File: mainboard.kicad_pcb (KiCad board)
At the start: 4 copper layers, 94.4 x 36.2 mm, 48 parts, among them IC1 BMX160, J1 Conn_01x01, J2 10118194-0001LF, J28 Conn_01x01, J29 Conn_01x01, J3 Micro_SD_Card, J30 Conn_01x01, J4 xf2m-2415-1a, J5 XF2M-1015-1A, SW1 KMR231NG LFS, U1 RFM95W-915S2, U2 ATSAMD51G_TQFN48, U3 DRV8848, U4 TPS82740BSIPR, U5 DRV8848, U6 MAX708RESA-T, U8 RFM95W-915S2, X1 ANTENNA_U.FL, X2 ANTENNA_U.FL

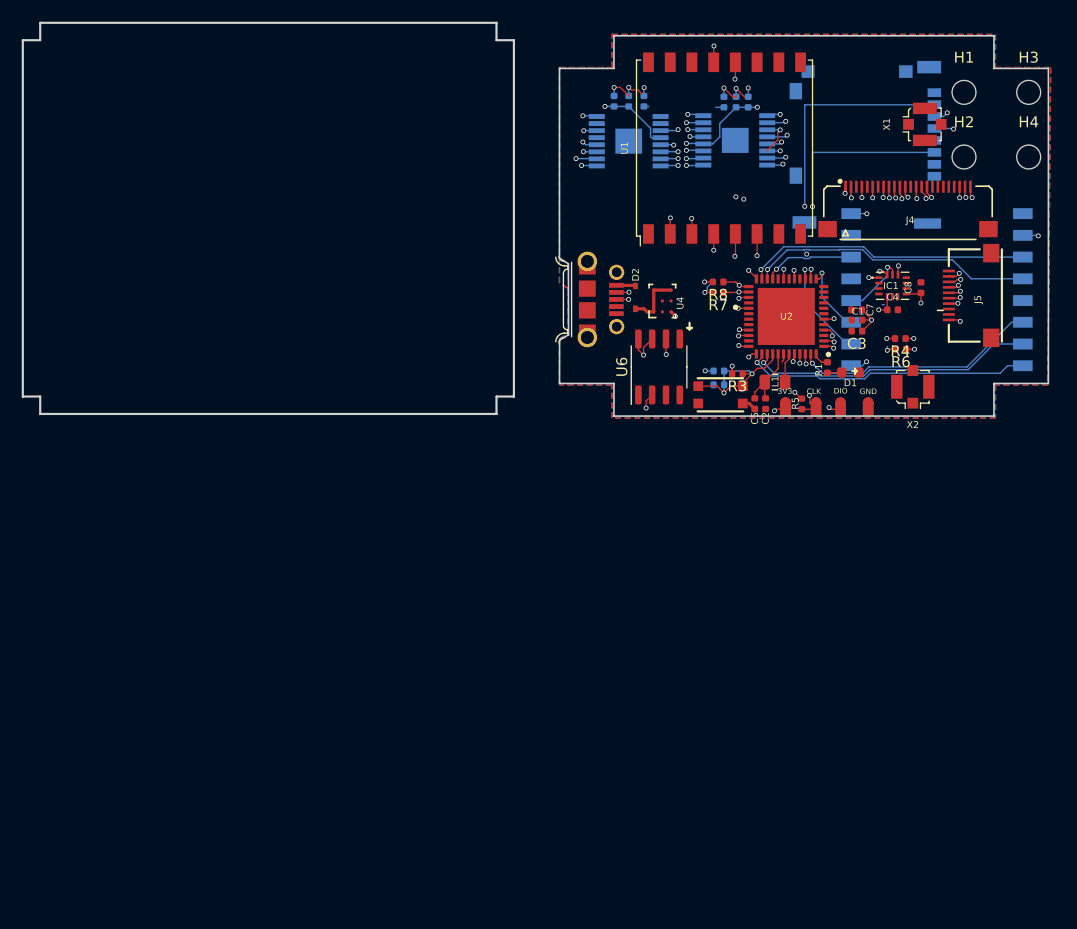
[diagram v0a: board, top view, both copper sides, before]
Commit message: modified board outline based on update from mechanical, including USB slot
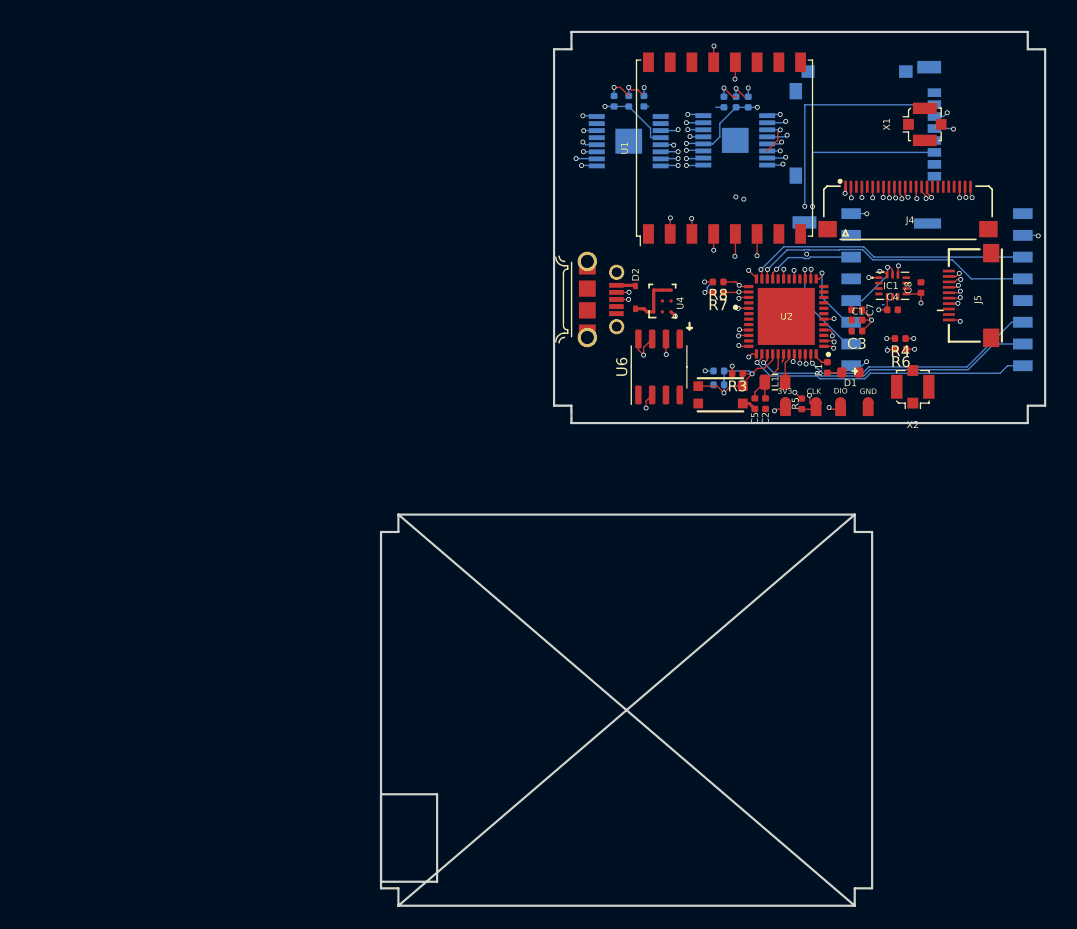
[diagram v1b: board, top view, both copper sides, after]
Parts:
- removed H1, H2, H3, H4: MountingHole, MountingHole:MountingHole_2.2mm_M2
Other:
- board size 94.4 x 36.2 mm -> 61.1 x 80.4 mm

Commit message: updated edge cuts to match updated mechanical .dxf file (to allow flat flex connectors to travel around board edge)
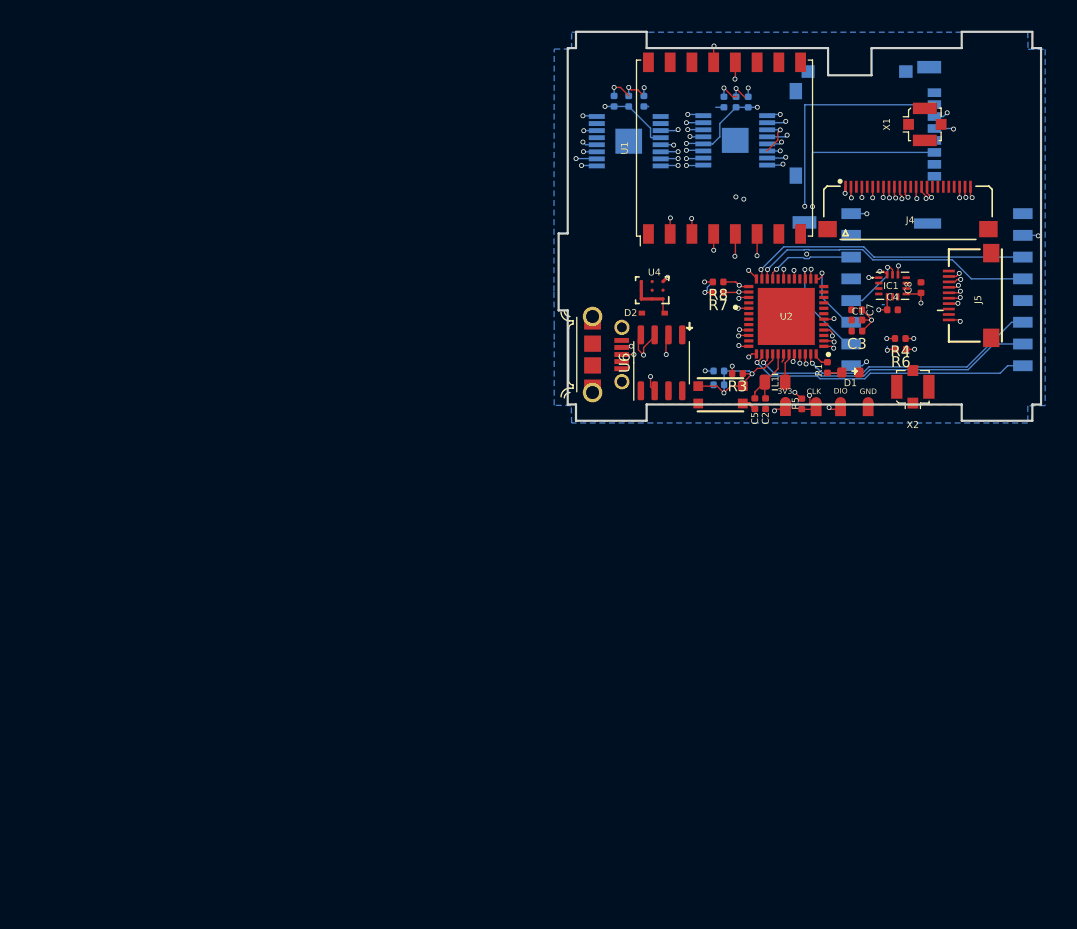
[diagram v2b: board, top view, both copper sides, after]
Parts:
- moved J2 5.09 mm to (79.8, 103.4)
- moved D2 2.19 mm to (85.3, 99.6), turned to 180 degrees
- moved U4 1.37 mm to (85.2, 97.5), turned to 180 degrees
- moved U6 0.44 mm to (86.1, 104.1)
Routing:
- net VUSB: track 1.78 -> 0.45 mm
- net /USB+: track 13.8 -> 12.7 mm
- net /USB-: track 14.1 -> 13.1 mm
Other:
- board size 61.1 x 80.4 mm -> 44.4 x 35.8 mm

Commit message: Updated component placement on top and bottom faces (no traces)
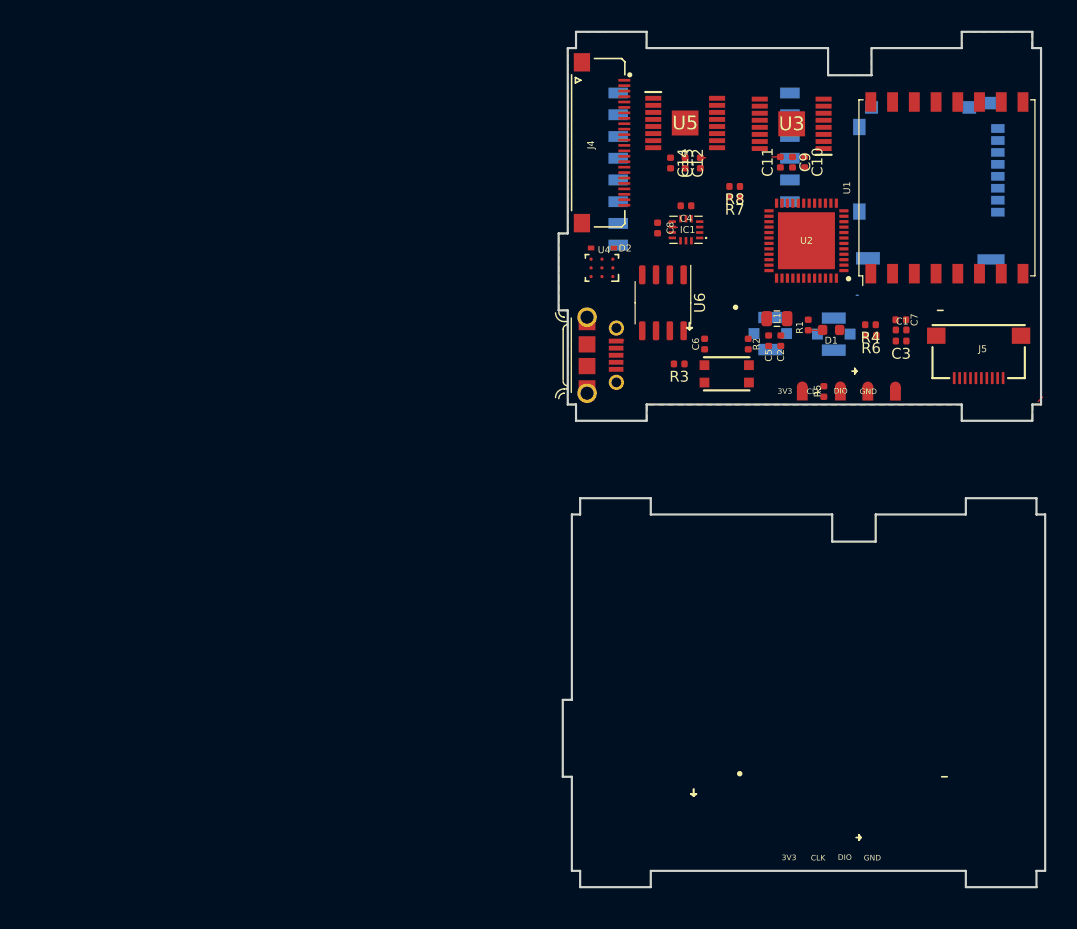
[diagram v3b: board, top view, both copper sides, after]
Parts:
- C10, C11, C12, C13, C14, C6, C9, R2, U3, U5: moved to F.Cu
- X1, X2: moved to B.Cu
- moved J4 26.4 mm to (82.7, 83.9), turned to 270 degrees
- moved C8 24.9 mm to (85.7, 91.7), turned to 270 degrees
- moved U8 24.1 mm to (90.0, 86.3)
- moved X1 23.9 mm to (96.1, 101.4), turned to 90 degrees
- moved C4 21.3 mm to (88.4, 89.7), turned to 180 degrees
- moved U1 20.8 mm to (112.4, 88.0)
- moved IC1 19.7 mm to (88.4, 91.9), turned to 0 degrees
- moved R7 8.92 mm to (92.8, 88.9)
- moved R8 8.92 mm to (92.8, 87.9)
- moved X2 8.75 mm to (102.0, 101.5), turned to 270 degrees
- moved J5 8.09 mm to (115.3, 105.5), turned to 180 degrees
- moved C12 7.70 mm to (88.3, 85.8), turned to 270 degrees
- moved C13 7.70 mm to (89.7, 85.8), turned to 90 degrees
- moved C14 7.70 mm to (86.9, 85.8), turned to 270 degrees
- moved D2 7.60 mm to (80.7, 93.6), turned to 0 degrees
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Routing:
- net BATT_P: track 72.4 -> 0.07 mm, vias 5 -> 0
- net MISO: track 68.2 -> 0.00 mm, vias 5 -> 0
- net MOSI: track 57.7 -> 0.00 mm, vias 5 -> 0
- net SCK: track 49.5 -> 0.00 mm, vias 6 -> 0
- net MOY_2: track 31.4 -> 0.00 mm, vias 2 -> 0
- net MOY_1: track 30.7 -> 0.04 mm, vias 2 -> 0
- net +3V3: track 30.9 -> 1.85 mm, vias 21 -> 0
- net GND: track 29.5 -> 0.64 mm, vias 17 -> 0
- net RF_DIO1: track 26.6 -> 0.00 mm, vias 1 -> 0
- net RF_DIO2: track 26.5 -> 0.00 mm, vias 1 -> 0
- net RF_BUSY: track 26.3 -> 0.00 mm, vias 1 -> 0
- net RF_DIO3: track 26.3 -> 0.00 mm, vias 1 -> 0
- net SDA1: track 25.2 -> 0.00 mm, vias 3 -> 0
- net SCL1: track 23.9 -> 0.00 mm, vias 3 -> 0
- net EN_CAM: track 22.9 -> 0.00 mm, vias 2 -> 0
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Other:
- board size 44.4 x 35.8 mm -> 44.8 x 78.7 mm

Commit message: updated layout with new camera connector placement, more traces, removed mounting holes
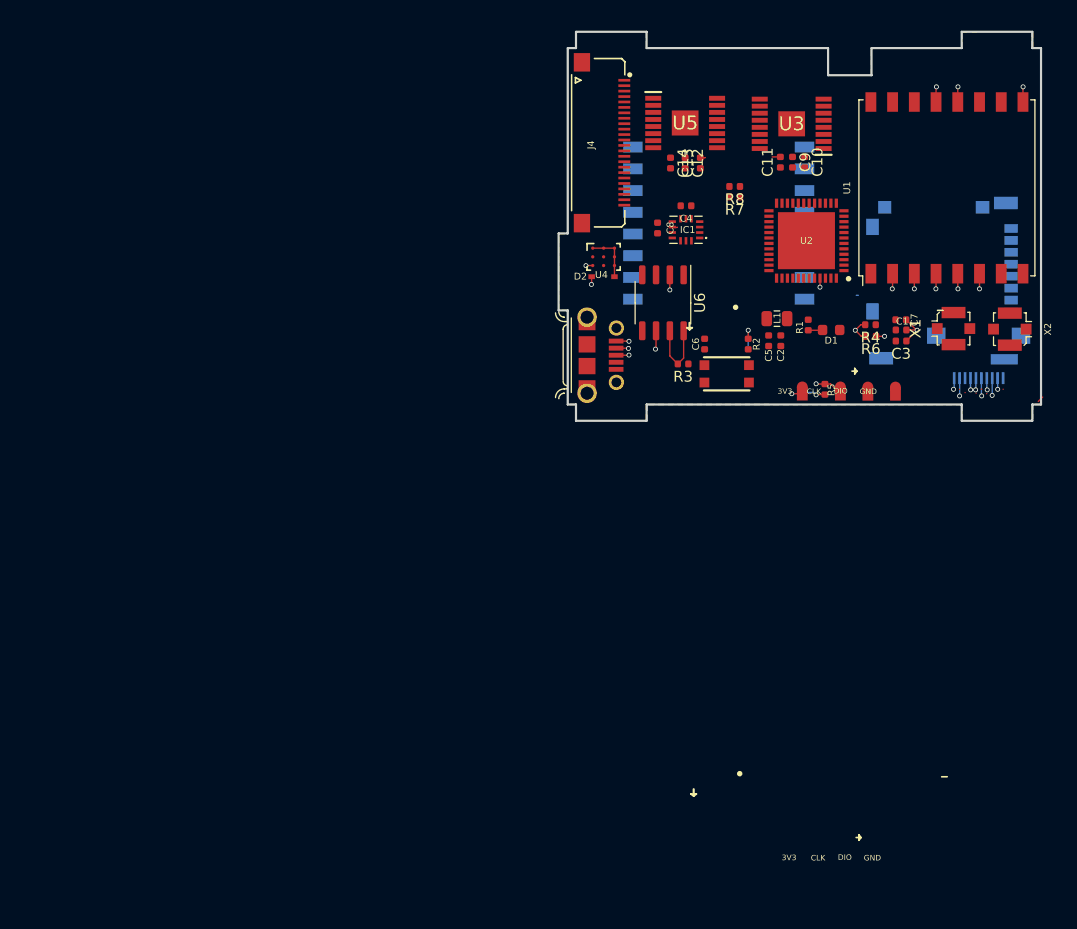
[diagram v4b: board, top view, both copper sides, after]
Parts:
- J5: moved to B.Cu
- X1, X2: moved to F.Cu
- moved X1 16.9 mm to (113.0, 101.0), turned to 270 degrees
- moved X2 16.2 mm to (118.2, 101.0), turned to 90 degrees
- moved J3 9.28 mm to (112.7, 96.6)
- moved U8 5.15 mm to (91.4, 91.3)
- moved D2 2.64 mm to (80.7, 96.2), turned to 180 degrees
- moved U4 1.03 mm to (80.8, 94.4), turned to 0 degrees
- moved R3 0.36 mm to (88.1, 104.2)
- moved R5 0.23 mm to (101.1, 106.6), turned to 90 degrees
- moved R6 0.08 mm to (105.4, 101.7)
- turned J5 to 0 degrees
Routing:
- net +3V3: track 1.85 -> 17.2 mm, vias 0 -> 8
- net Net-(R3-Pad2): track 0.00 -> 6.63 mm
- net Net-(D2-Pad1): track 0.00 -> 4.63 mm
- net /SWCLK: track 0.00 -> 3.44 mm, vias 0 -> 2
- net MOSI: track 0.00 -> 2.99 mm, vias 0 -> 2
- net MISO: track 0.00 -> 2.50 mm, vias 0 -> 2
- net SCK: track 0.00 -> 2.44 mm, vias 0 -> 2
- net WDT_WDI: track 0.00 -> 1.71 mm, vias 0 -> 1
- net CS_CAM: track 0.00 -> 1.65 mm, vias 0 -> 1
- net GND: track 0.64 -> 2.28 mm, vias 0 -> 1
- net VUSB: track 0.45 -> 1.91 mm, vias 0 -> 2
- net RF2_BUSY: track 0.00 -> 1.40 mm, vias 0 -> 1
- net CS_RF2: track 0.00 -> 1.40 mm, vias 0 -> 1
- net Net-(U1-Pad9): track 0.00 -> 1.40 mm, vias 0 -> 1
- net RF2_RST: track 0.00 -> 1.40 mm, vias 0 -> 1
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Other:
- board size 44.8 x 78.7 mm -> 44.4 x 35.8 mm

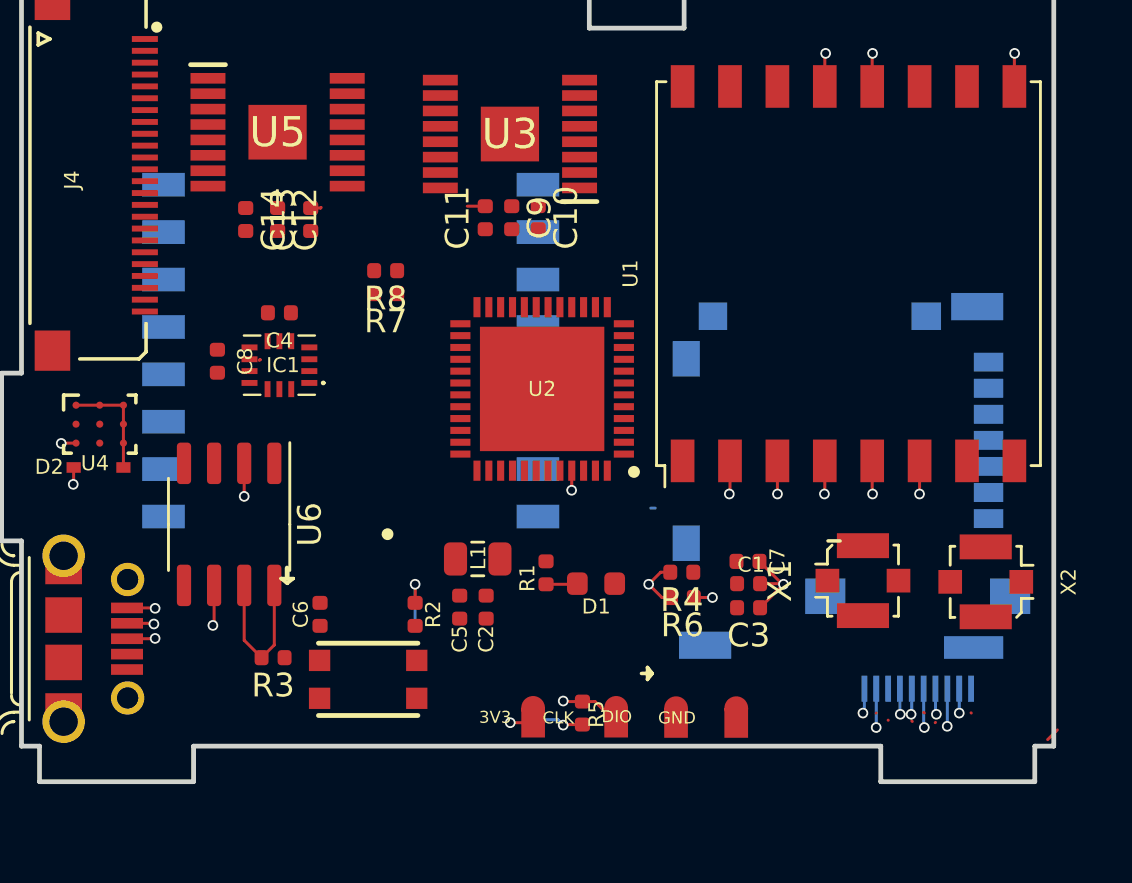
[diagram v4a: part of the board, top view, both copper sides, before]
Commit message: updated footprints for U.FL connectors, more traces added
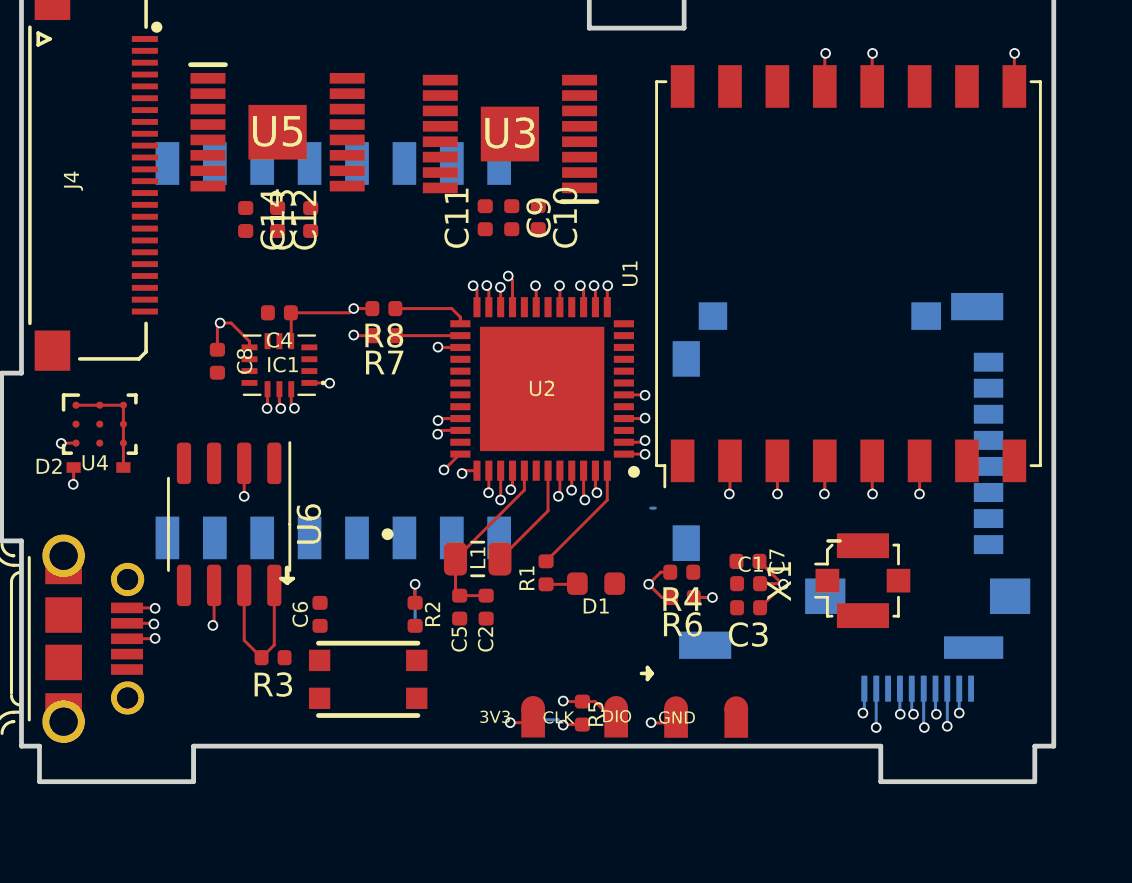
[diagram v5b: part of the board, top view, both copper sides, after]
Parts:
- removed X2: ANTENNA_U.FL, Connector_Coaxial:U.FL_Molex_MCRF_73412-0110_Vertical
- moved R7 1.78 mm to (92.8, 90.7)
- moved R8 1.60 mm to (92.8, 89.5)
- moved U8 0.74 mm to (90.6, 91.3), turned to 90 degrees
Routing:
- net +3V3: track 17.2 -> 29.2 mm, vias 8 -> 16
- net Net-(C2-Pad1): track 0.00 -> 7.67 mm
- net /LED1: track 0.00 -> 4.90 mm
- net Net-(L1-Pad1): track 0.00 -> 4.57 mm
- net SCL2: track 0.00 -> 3.17 mm
- net SDA2: track 0.06 -> 2.78 mm
- net /SWDIO: track 0.00 -> 2.32 mm, vias 0 -> 2
- net MISO: track 2.50 -> 4.33 mm, vias 2 -> 4
- net MOSI: track 2.99 -> 4.76 mm, vias 2 -> 4
- net CS_IMU: track 0.00 -> 1.78 mm, vias 0 -> 2
- net SCK: track 2.44 -> 4.21 mm, vias 2 -> 4
- net RF_RST: track 0.00 -> 1.39 mm, vias 0 -> 1
- net RF_DIO1: track 0.00 -> 1.24 mm, vias 0 -> 1
- net /USB+: track 1.19 -> 2.22 mm, vias 1 -> 2
- net /USB-: track 1.15 -> 2.13 mm, vias 1 -> 2
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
